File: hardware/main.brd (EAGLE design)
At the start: 96.5 x 65.5 mm, 94 parts, among them SW1 USER_SLIDE, SW2 USER_SLIDE, U1 TMS320F28069_PN_80, U10 TXB0101_DBV_6, U2 SN74LVC4245A_DW_24, U3 Value, U4 SN74LVC4245A_DW_24, U5 Value, U6 SN74ABT541B_DW_20, U7 SN74LVC1G04_DBV_5, U8 SST25VF080BS2AF, U9 TXB0101_DBV_6

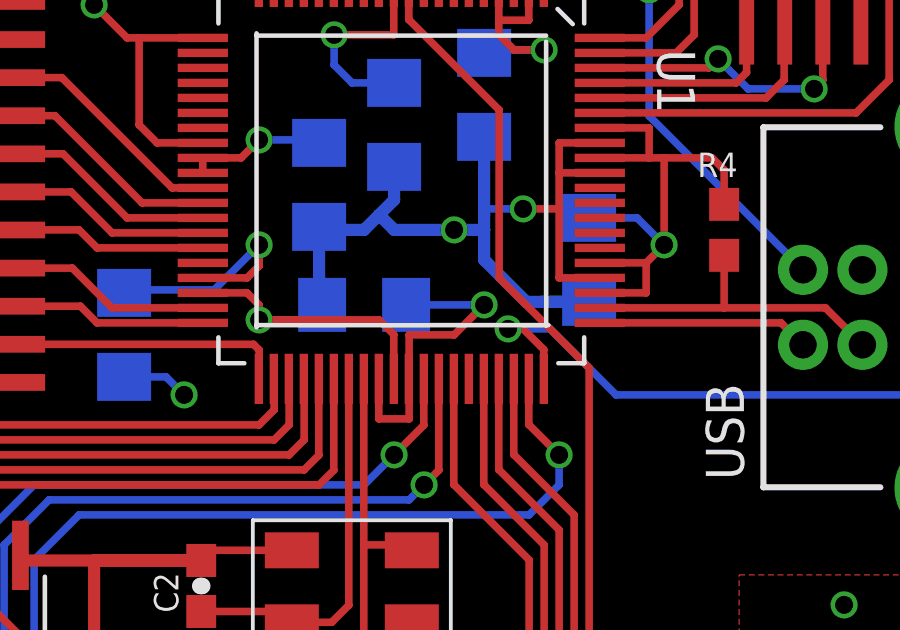
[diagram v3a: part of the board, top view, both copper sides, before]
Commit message: DRC fixes with extra room
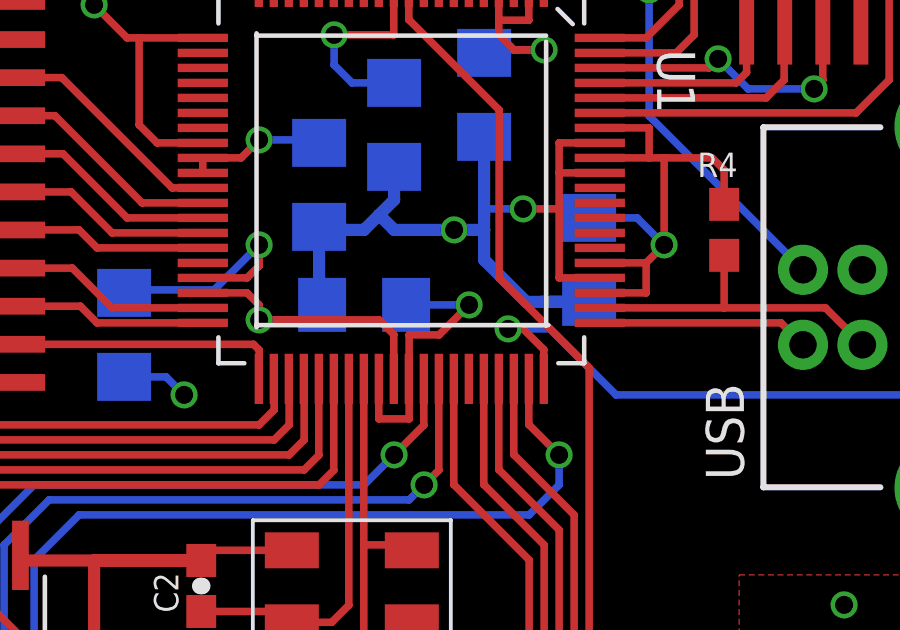
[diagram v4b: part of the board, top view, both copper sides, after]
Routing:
- net 3.3V: track 164.4 -> 163.4 mm
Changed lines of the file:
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@@
 <layers>
 <layer number="1" name="Top" color="4" fill="1" visible="yes" active="yes"/>
-<layer number="2" name="Route2" color="1" fill="3" visible="no" active="yes"/>
+<layer number="2" name="Route2" color="1" fill="3" visible="yes" active="yes"/>
 <layer number="3" name="Route3" color="4" fill="3" visible="no" active="no"/>
 <layer number="4" name="Route4" color="1" fill="4" visible="no" active="no"/>
@@
 <layer number="13" name="Route13" color="4" fill="5" visible="no" active="no"/>
 <layer number="14" name="Route14" color="1" fill="6" visible="no" active="no"/>
-<layer number="15" name="Route15" color="4" fill="6" visible="no" active="yes"/>
+<layer number="15" name="Route15" color="4" fill="6" visible="yes" active="yes"/>
 <layer number="16" name="Bottom" color="1" fill="1" visible="yes" active="yes"/>
 <layer number="17" name="Pads" color="2" fill="1" visible="yes" active="yes"/>
@@
 </class>
 </classes>
-<designrules name="Elecrow_4-layer_PCB_eagle_rule">
+<designrules name="Elecrow_4-layer_PCB_eagle_rule *">
 <description language="de">&lt;b&gt;EAGLE Design Rules&lt;/b&gt;
 &lt;p&gt;
@@
 <param name="mtCopper" value="0.035mm 0.035mm 0.035mm 0.035mm 0.035mm 0.035mm 0.035mm 0.035mm 0.035mm 0.035mm 0.035mm 0.035mm 0.035mm 0.035mm 0.035mm 0.035mm"/>
 <param name="mtIsolate" value="0.2mm 1.2mm 0.2mm 0.15mm 0.2mm 0.15mm 0.2mm 0.15mm 0.2mm 0.15mm 0.2mm 0.15mm 0.2mm 0.15mm 0.2mm"/>
-<param name="mdWireWire" value="6mil"/>
-<param name="mdWirePad" value="6mil"/>
-<param name="mdWireVia" value="6mil"/>
-<param name="mdPadPad" value="6mil"/>
-<param name="mdPadVia" value="6mil"/>
-<param name="mdViaVia" value="8mil"/>
+<param name="mdWireWire" value="8mil"/>
+<param name="mdWirePad" value="8mil"/>
+<param name="mdWireVia" value="8mil"/>
+<param name="mdPadPad" value="8mil"/>
+<param name="mdPadVia" value="8mil"/>
+<param name="mdViaVia" value="10mil"/>
 <param name="mdSmdPad" value="0mil"/>
 <param name="mdSmdVia" value="0mil"/>
@@
 <param name="mdViaViaSameLayer" value="8mil"/>
 <param name="mnLayersViaInSmd" value="2"/>
-<param name="mdCopperDimension" value="20mil"/>
-<param name="mdDrill" value="10mil"/>
+<param name="mdCopperDimension" value="22mil"/>
+<param name="mdDrill" value="12mil"/>
 <param name="mdSmdStop" value="0mil"/>
-<param name="msWidth" value="6mil"/>
-<param name="msDrill" value="12mil"/>
-<param name="msMicroVia" value="12mil"/>
+<param name="msWidth" value="10mil"/>
+<param name="msDrill" value="14mil"/>
+<param name="msMicroVia" value="14mil"/>
 <param name="msBlindViaRatio" value="0.5"/>
 <param name="rvPadTop" value="0.25"/>
@@
 <wire x1="81" y1="37.5" x2="80.1" y2="38.4" width="0.254" layer="16"/>
 <wire x1="80.1" y1="38.4" x2="78.5" y2="38.4" width="0.254" layer="16"/>
-<wire x1="72.5" y1="34.5" x2="74" y2="34.5" width="0.254" layer="1"/>
-<wire x1="74" y1="34.5" x2="75" y2="35.5" width="0.254" layer="1"/>
-<via x="75" y="35.5" extent="1-16" drill="0.6"/>
-<wire x1="75" y1="35.5" x2="72.4" y2="35.5" width="0.254" layer="16"/>
+<wire x1="72.5" y1="34.5" x2="73.5" y2="34.5" width="0.254" layer="1"/>
+<wire x1="73.5" y1="34.5" x2="74.5" y2="35.5" width="0.254" layer="1"/>
+<via x="74.5" y="35.5" extent="1-16" drill="0.6"/>
+<wire x1="74.5" y1="35.5" x2="72.4" y2="35.5" width="0.254" layer="16"/>
 <wire x1="72.4899875" y1="33.0333" x2="72.5" y2="33.0433125" width="0.254" layer="1"/>
 <wire x1="72.5" y1="33.0433125" x2="72.5" y2="34.5" width="0.254" layer="1"/>

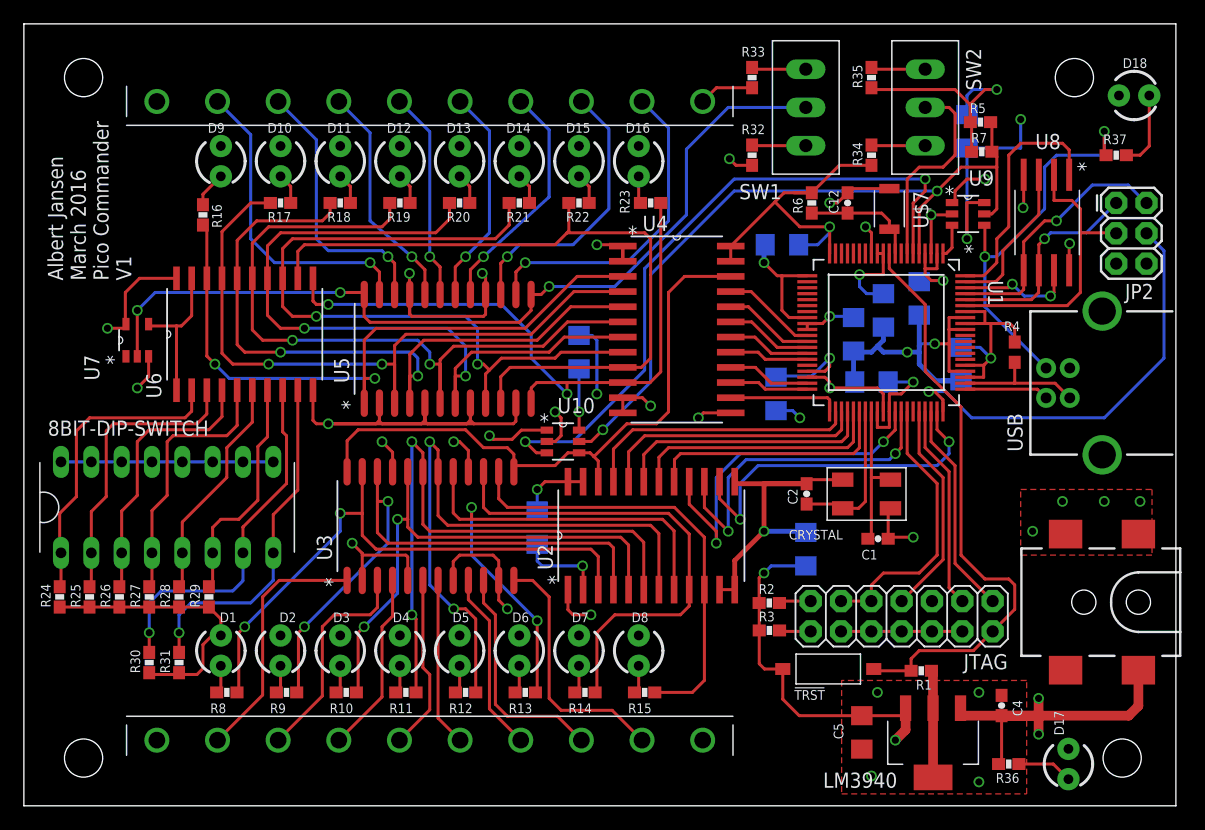
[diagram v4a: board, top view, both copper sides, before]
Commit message: Final of v1. Sent to fab house. DRC and minor silkscreen updates
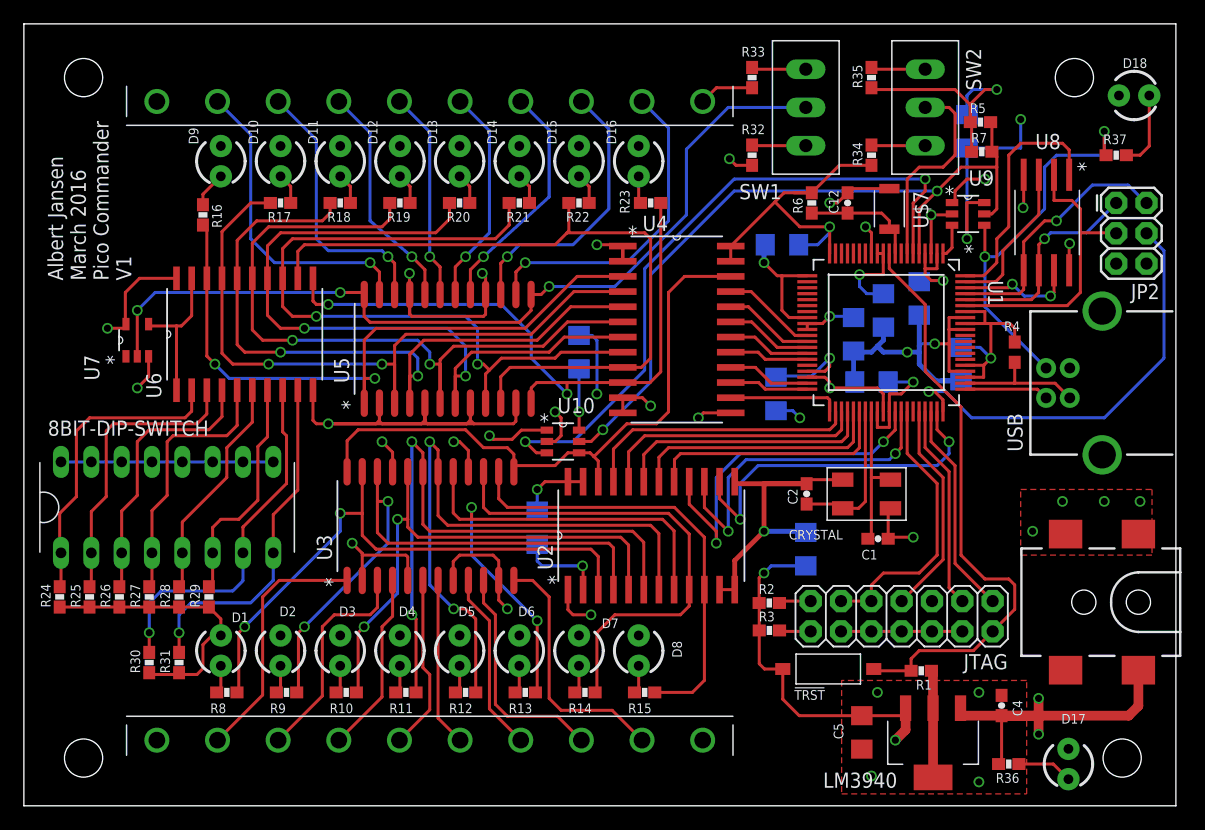
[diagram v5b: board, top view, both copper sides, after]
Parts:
- R6: value 47K -> 10K

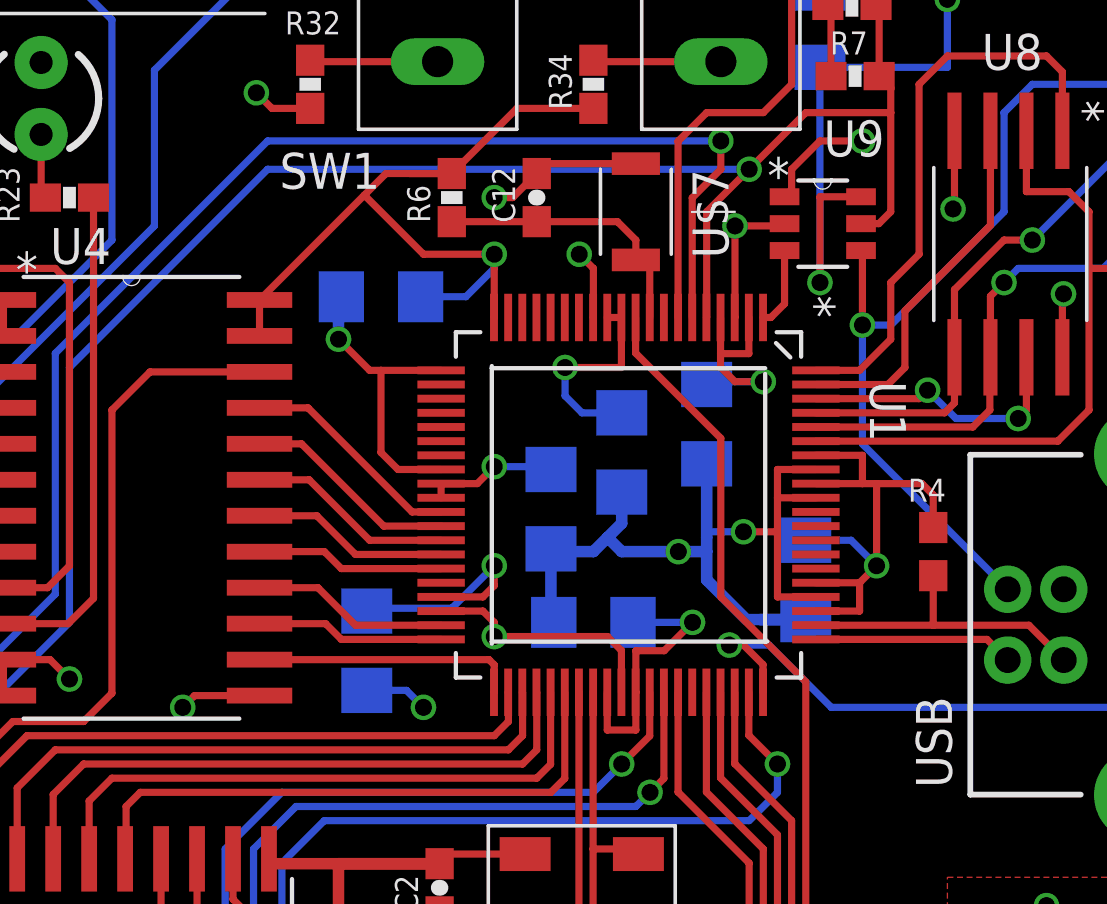
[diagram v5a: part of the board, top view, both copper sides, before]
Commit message: Updated connections to include nets. Fixed connection problem between VDD and VDDIO pins
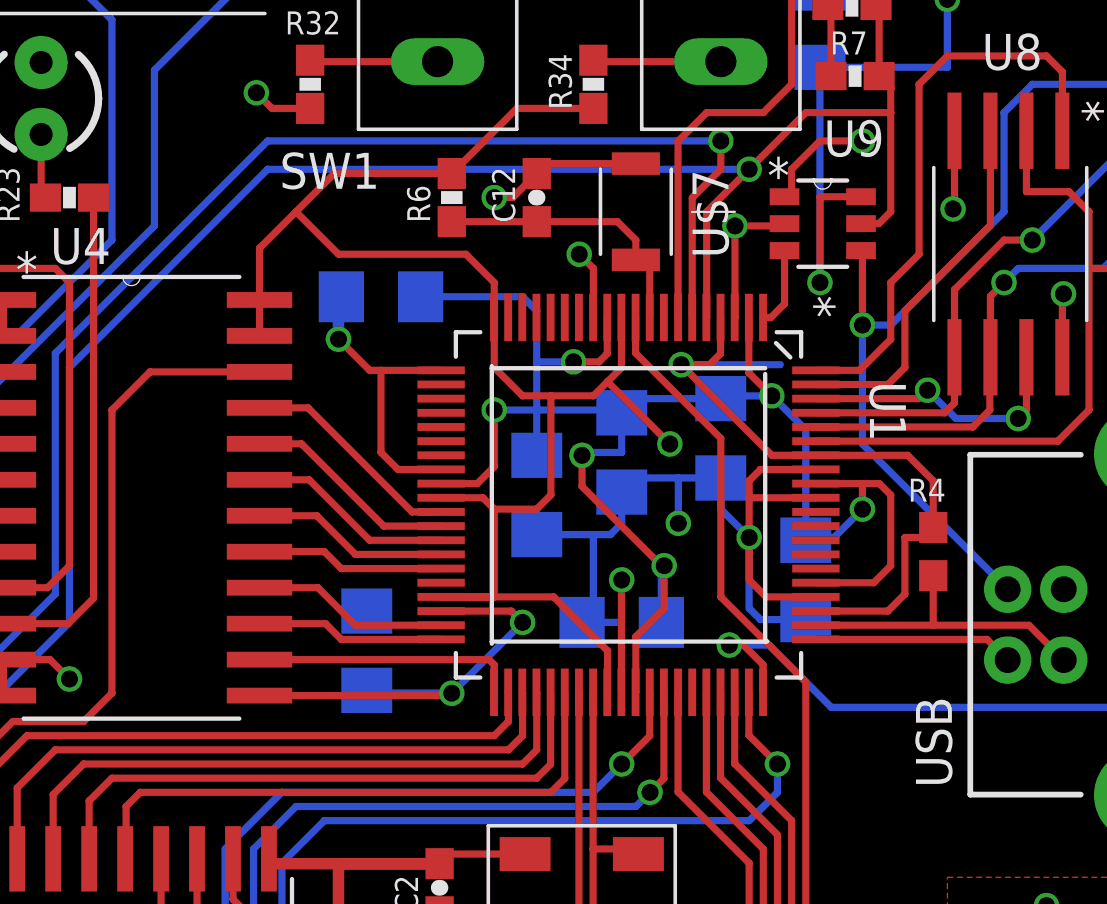
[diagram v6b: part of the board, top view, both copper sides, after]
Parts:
- moved C11 1.00 mm to (72.0, 35.5)
- moved C6 0.71 mm to (75.5, 42.0)
- moved C8 0.71 mm to (69.0, 40.0)
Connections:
- new net VDD: C10.1, C11.1, C3.1, C6.1, C8.1, C9.1, U1.12, U1.2, U1.29, U1.51, U1.65, U1.72
- net 3.3V: no longer C10.1, C11.1, C3.1, C6.1, C7.1, C8.1, C9.1, U1.12, U1.2, U1.29, U1.51, U1.65, U1.72
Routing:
- net VDD: track 0.00 -> 62.8 mm, vias 0 -> 6
- net GND: track 274.8 -> 281.0 mm
- net 3.3V: track 163.4 -> 163.0 mm, vias 13 -> 8
